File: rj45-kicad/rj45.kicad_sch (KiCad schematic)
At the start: 46 parts

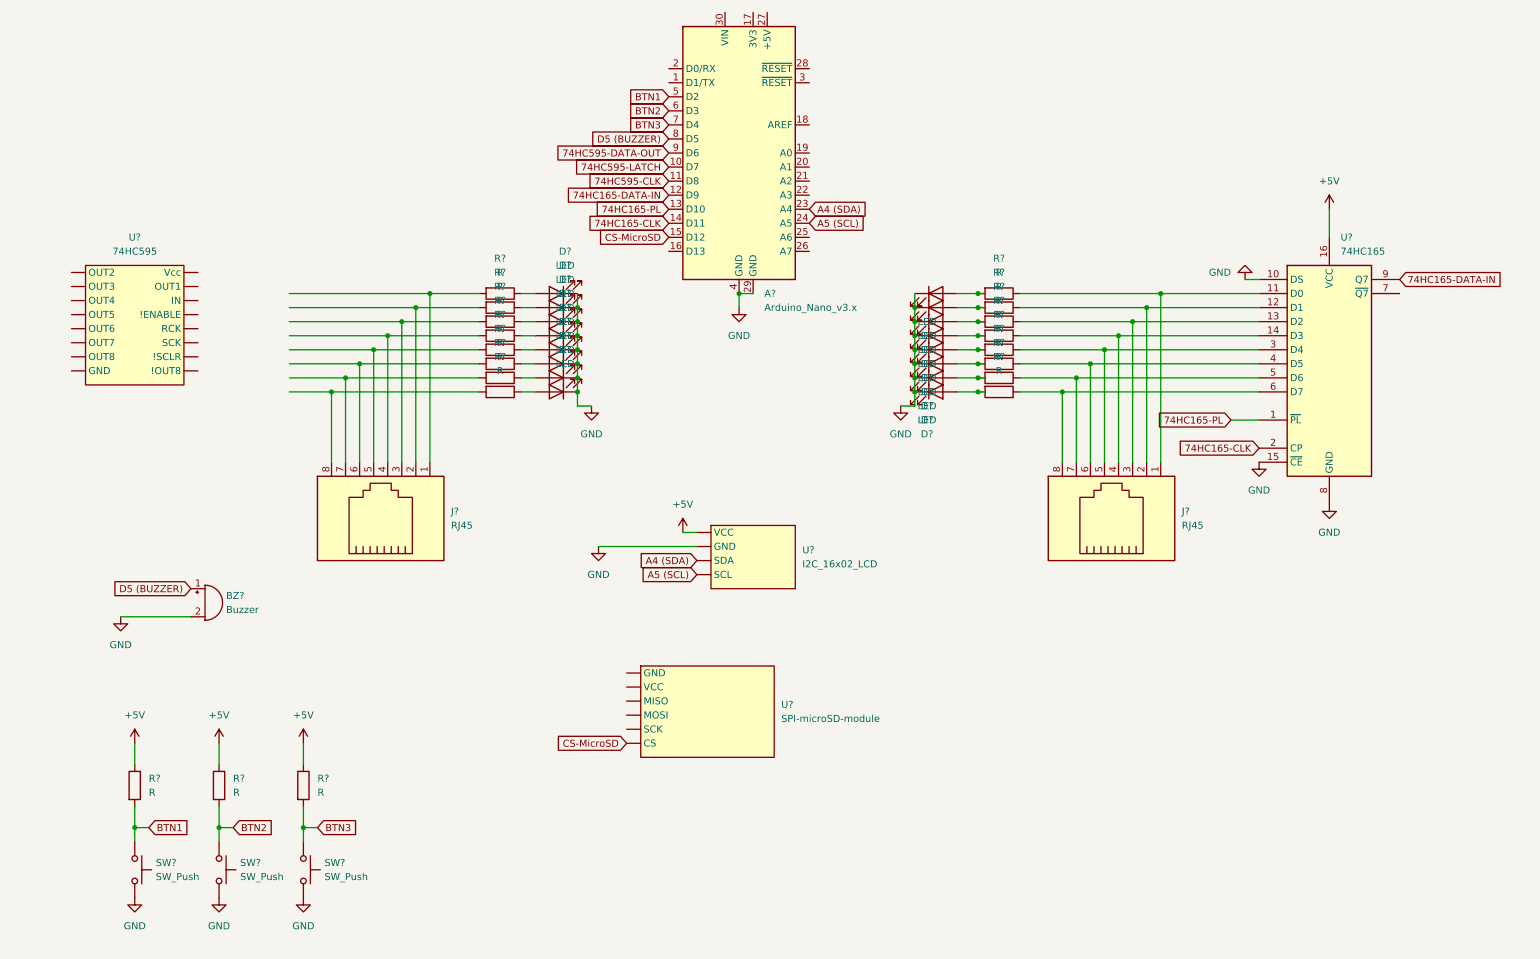
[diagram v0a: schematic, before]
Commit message: Buttons with low-pass filters
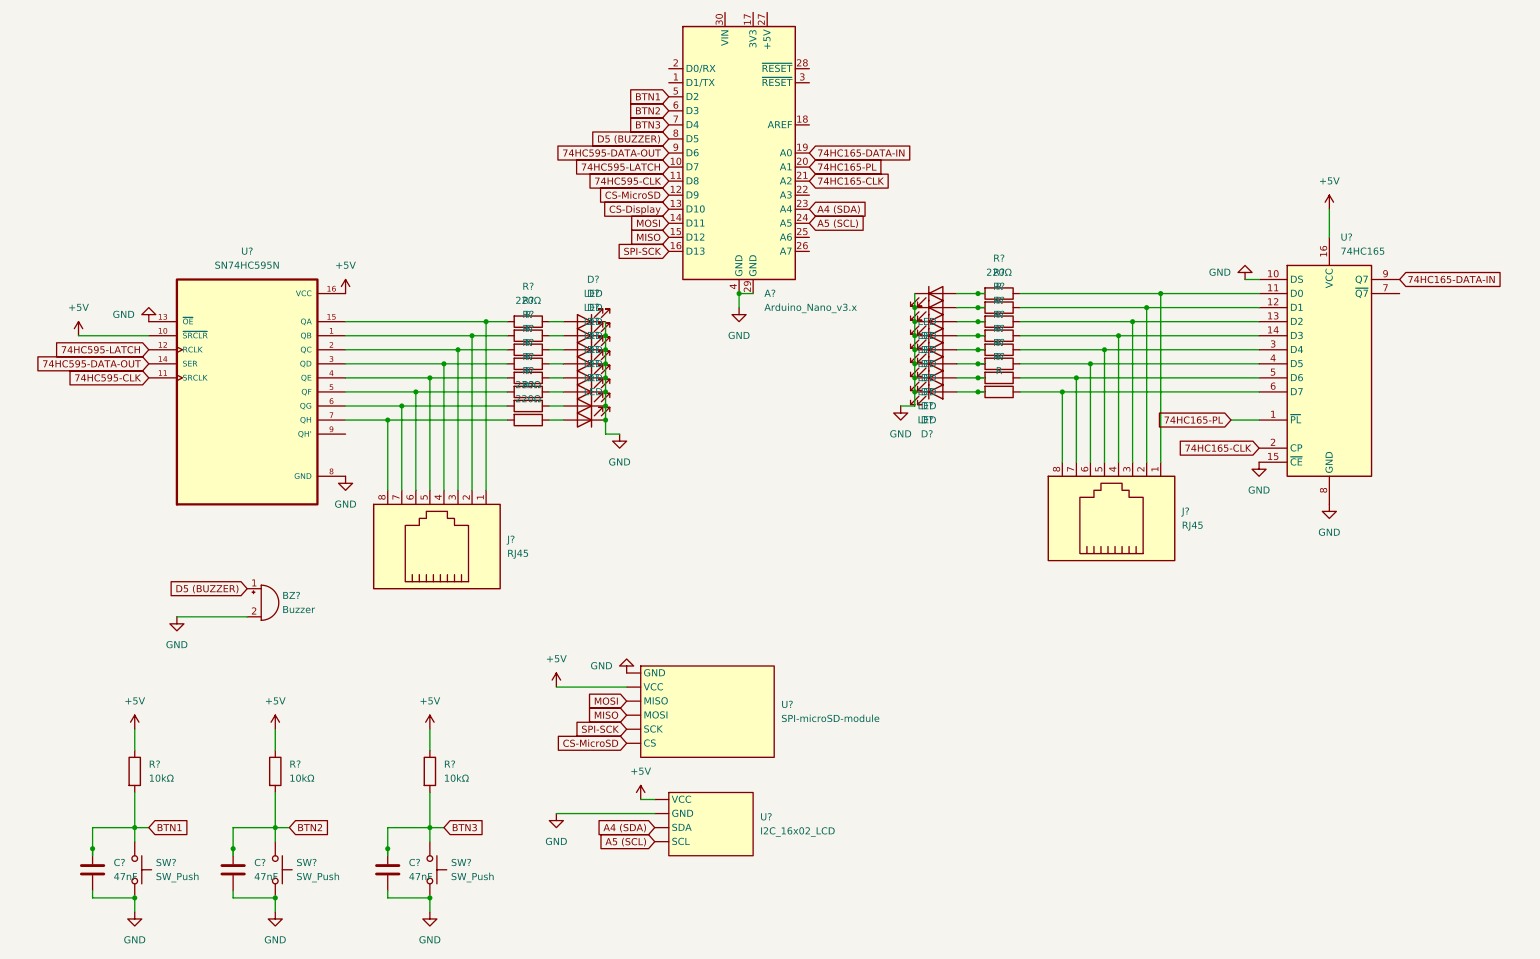
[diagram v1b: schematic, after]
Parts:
- removed R? (x2): R, symbol Device:R
- removed SW? (x2): SW_Push, symbol Switch:SW_Push
- removed U?: 74HC595, symbol custom-parts:74HC595
- added C? (x3): 47nF, symbol Device:C
- added R? (x2): 10kΩ, symbol Device:R
- added SW? (x2): SW_Push, symbol Switch:SW_Push
- added U?: SN74HC595N, SN74HC595N:DIP794W45P254L1969H508Q16, symbol SN74HC595N:SN74HC595N
- R? (x4): value R -> 220Ω
- R?: value R -> 10kΩ
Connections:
- net +5V: now also U?. (VCC), R?.1, R?.1, U?.10 (~{SRCLR}), U?.16 (VCC)
- net 74HC165-CLK: now also A?.21 (A2); no longer A?.14 (D11)
- net 74HC165-DATA-IN: now also A?.19 (A0); no longer A?.12 (D9)
- net 74HC165-PL: now also A?.20 (A1); no longer A?.13 (D10)
- net 74HC595-CLK: now also U?.11 (SRCLK)
- net 74HC595-DATA-OUT: now also U?.14 (SER)
- net 74HC595-LATCH: now also U?.12 (RCLK)
- net BTN1: now also C?.1
- net BTN2: now also C?.1, R?.2, SW?.1
- net BTN3: now also C?.1, R?.2, SW?.1
- net CS-MicroSD: now also A?.12 (D9); no longer A?.15 (D12)
- net GND: now also U?. (VCC), C?.2, C?.2, C?.2, SW?.2, SW?.2, U?.13 (~{OE}), U?.8 (GND)
- net SPI-SCK: now reaches A?.16 (D13)
- net SPI-SCK: now also U?. (VCC)
- net at J?.8, R?.2: now also U?.7 (QH)
- net at J?.4, R?.2: now also U?.3 (QD)
- net at J?.1, R?.2: now also U?.15 (QA)
- net at J?.2, R?.2: now also U?.1 (QB)
- net at J?.3, R?.2: now also U?.2 (QC)
- net at J?.5, R?.2: now also U?.4 (QE)
- net at J?.6, R?.2: now also U?.5 (QF)
- net at J?.7, R?.2: now also U?.6 (QG)
- new net CS-Display: A?.13 (D10)
- new net MISO: A?.15 (D12), U?. (VCC)
- new net MOSI: A?.14 (D11), U?. (VCC)
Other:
- moved on the sheet: BZ?, D?, J?, R?, U?
